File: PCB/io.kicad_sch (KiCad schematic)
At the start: 0 parts

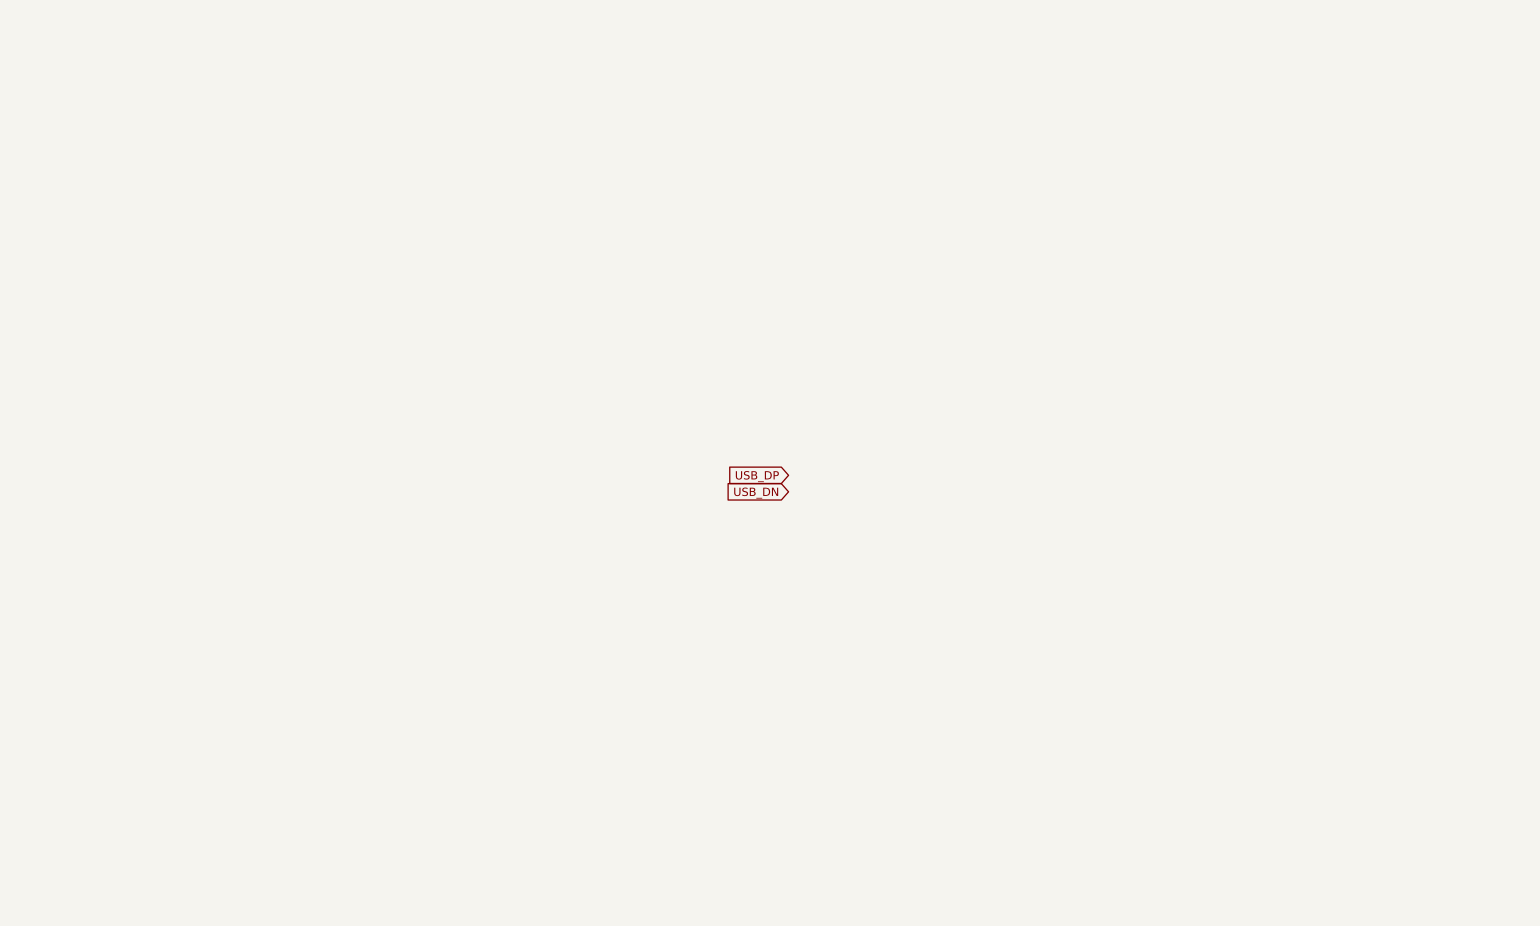
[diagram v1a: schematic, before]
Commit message: Added more components and added most needed values for the nrf example schematic
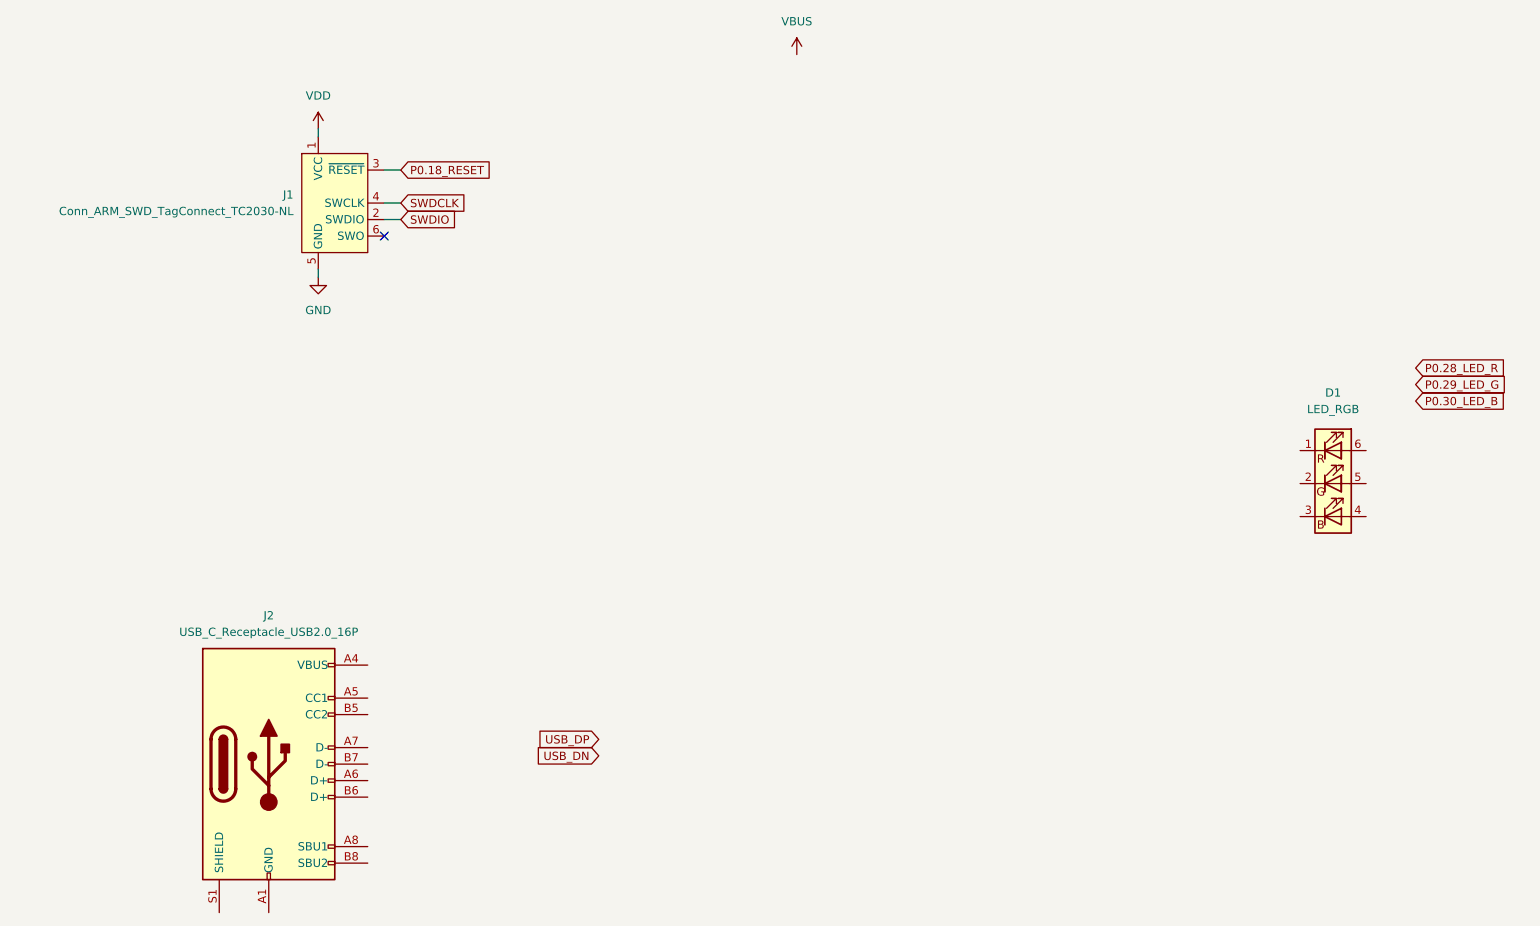
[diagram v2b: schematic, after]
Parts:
- added D1: LED_RGB, symbol Device:LED_RGB
- added J1: Conn_ARM_SWD_TagConnect_TC2030-NL, Connector:Tag-Connect_TC2030-IDC-NL_2x03_P1.27mm_Vertical, symbol Connector:Conn_ARM_SWD_TagConnect_TC2030-NL
- added J2: USB_C_Receptacle_USB2.0_16P, symbol Connector:USB_C_Receptacle_USB2.0_16P
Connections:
- new net: J2.A1 (GND), J2.A12 (GND), J2.B1 (GND), J2.B12 (GND)
- new net: J2.A4 (VBUS), J2.A9 (VBUS), J2.B4 (VBUS), J2.B9 (VBUS)
- new net GND: J1.5 (GND)
- new net P0.18_RESET: J1.3 (~{RESET})
- new net SWDCLK: J1.4 (SWCLK)
- new net SWDIO: J1.2 (SWDIO)
- new net VDD: J1.1 (VCC)
- no-connect marks 0 -> 1

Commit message: Added the Calathea Leaf as the outline and artwork for the project
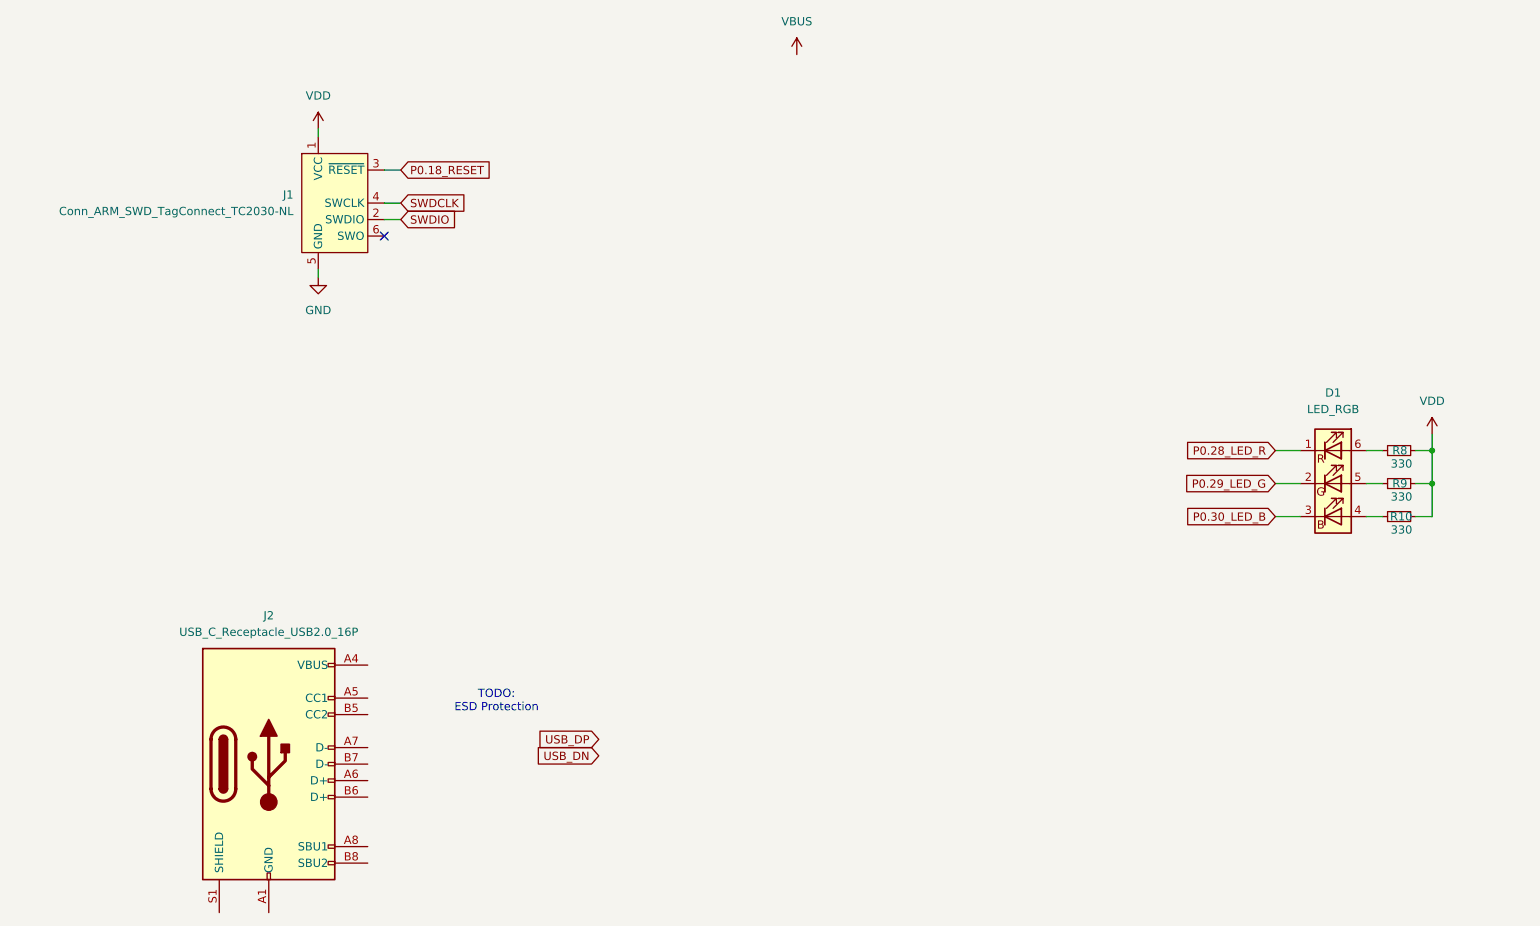
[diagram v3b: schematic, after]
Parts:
- added R10, R8, R9: 330, Resistor_SMD:R_0402_1005Metric, symbol Device:R_Small
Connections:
- net P0.28_LED_R: now also D1.1 (RK)
- net P0.29_LED_G: now also D1.2 (GK)
- net P0.30_LED_B: now also D1.3 (BK)
- net VDD: now also R10.2, R8.2, R9.2
- net at D1.4 (BA): now also R10.1
- net at D1.5 (GA): now also R9.1
- net at D1.6 (RA): now also R8.1
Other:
- note added: "TODO: ESD Protection"

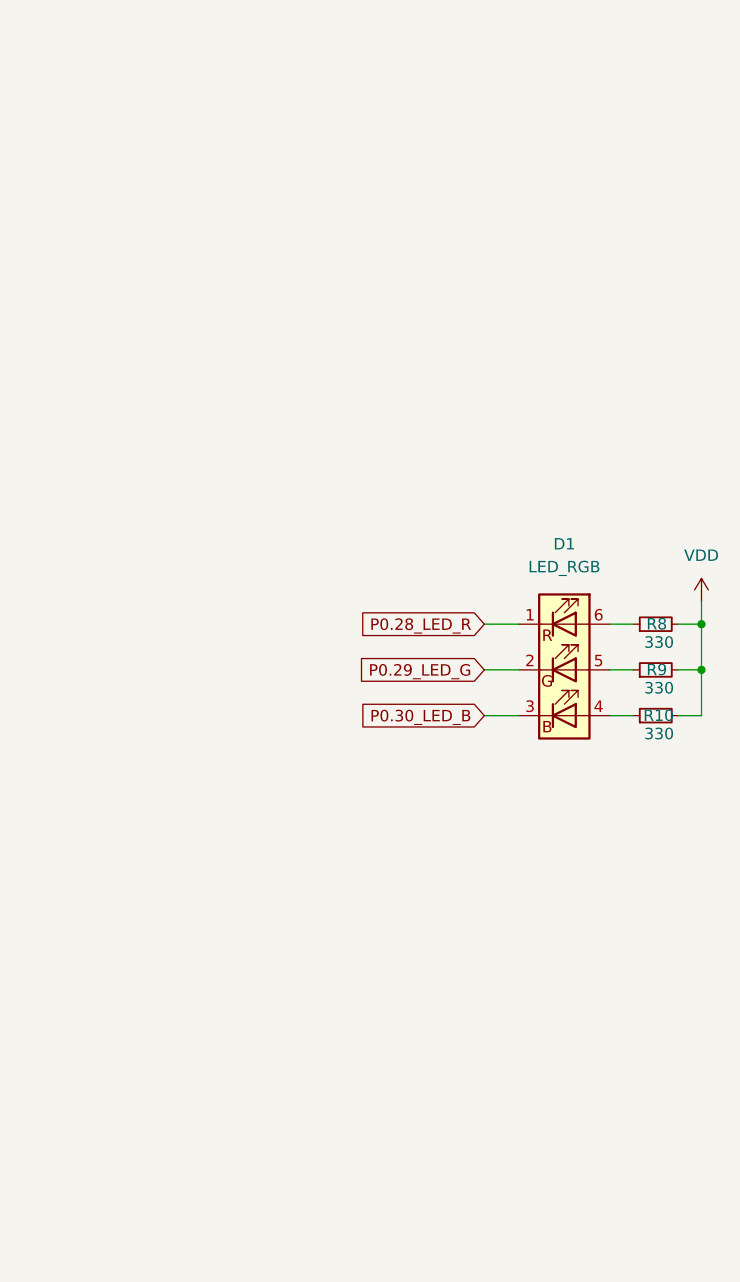
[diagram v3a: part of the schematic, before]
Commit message: Added LED Driver IC for the led bar inside the calathea leaf
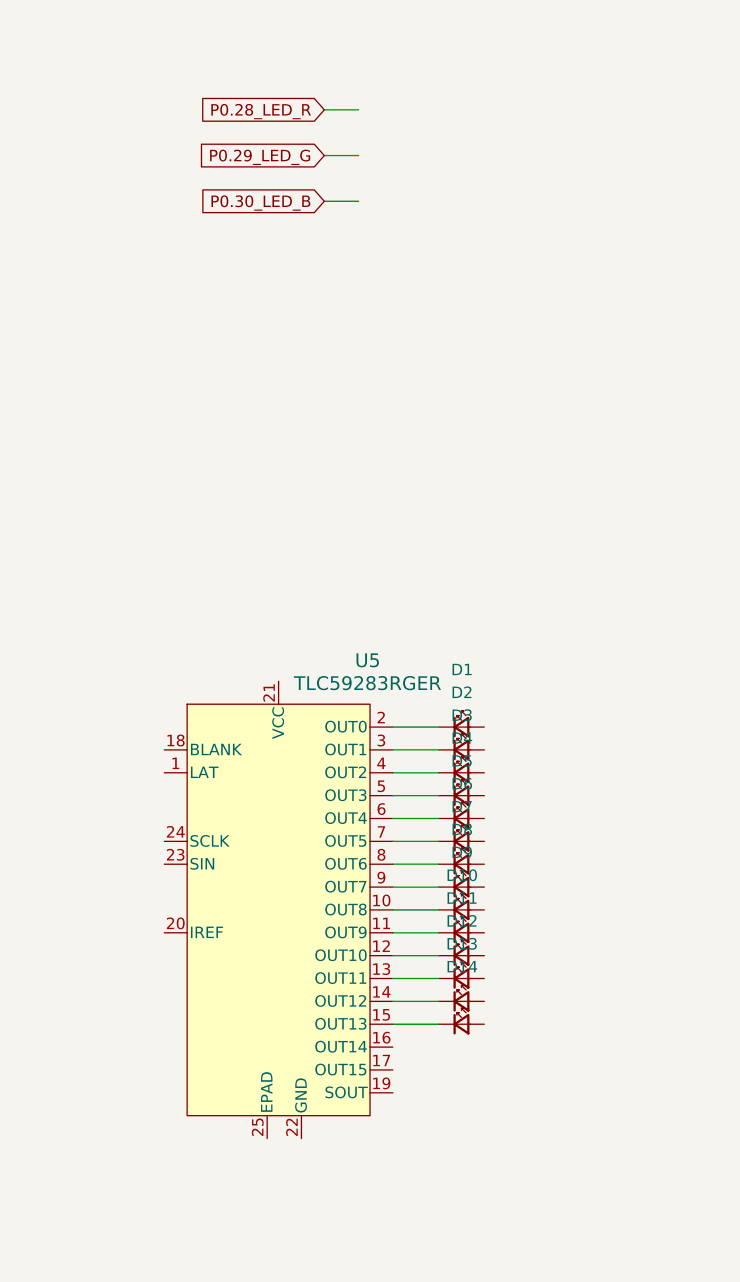
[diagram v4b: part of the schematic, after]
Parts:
- removed D1: LED_RGB, symbol Device:LED_RGB
- removed R10, R8, R9: 330, Resistor_SMD:R_0402_1005Metric, symbol Device:R_Small
- added D1, D10, D11, D12, D13, D14, D2, D3, D4, D5, D6, D7, D8, D9: LED_Small, LED_SMD:LED_0805_2012Metric, symbol Device:LED_Small
- added U5: TLC59283RGER, RGE24_2P1X2P1_TEX, symbol TLC59283:TLC59283RGER
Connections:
- new net: D7.1 (K), U5.8 (OUT6)
- new net: D8.1 (K), U5.9 (OUT7)
- new net: D6.1 (K), U5.7 (OUT5)
- new net: D3.1 (K), U5.4 (OUT2)
- new net: D5.1 (K), U5.6 (OUT4)
- new net: D1.1 (K), U5.2 (OUT0)
- new net: D2.1 (K), U5.3 (OUT1)
- new net: D9.1 (K), U5.10 (OUT8)
- new net: D10.1 (K), U5.11 (OUT9)
- new net: D11.1 (K), U5.12 (OUT10)
- new net: D12.1 (K), U5.13 (OUT11)
- new net: D13.1 (K), U5.14 (OUT12)
- new net: D14.1 (K), U5.15 (OUT13)
- new net: D4.1 (K), U5.5 (OUT3)

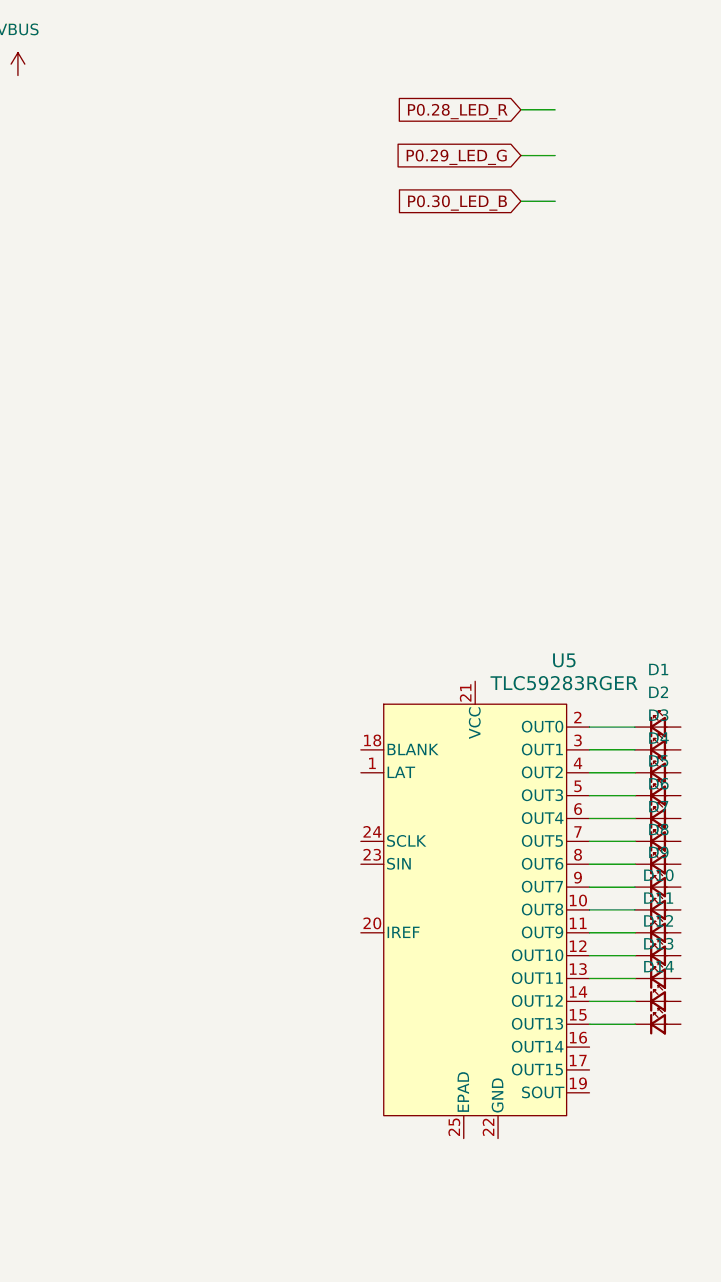
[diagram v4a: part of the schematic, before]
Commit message: added dcdc for external components. Changed board edge to a rect for easier dev board routuing.
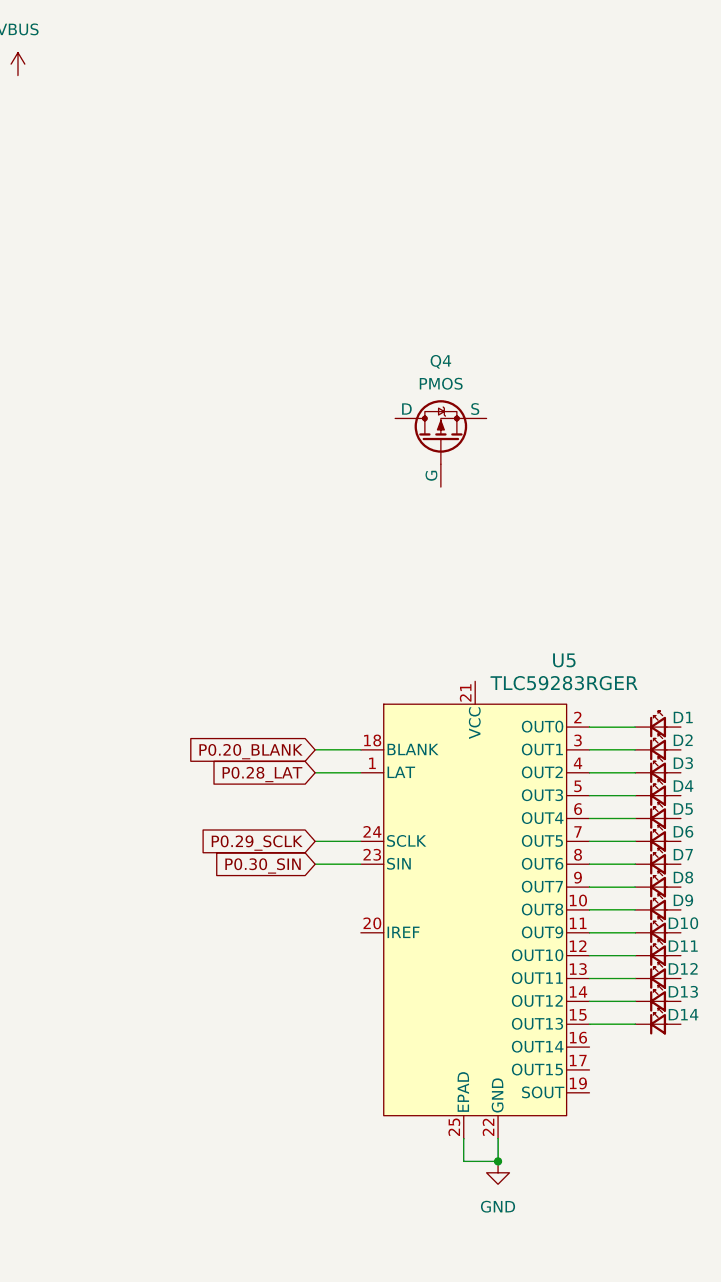
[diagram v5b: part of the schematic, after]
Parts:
- added Q4: PMOS, symbol Simulation_SPICE:PMOS
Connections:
- net GND: now also U5.22 (GND), U5.25 (EPAD)
- net P0.28_LAT: now reaches U5.1 (LAT)
- net P0.20_BLANK: now reaches U5.18 (BLANK)
- net P0.30_SIN: now reaches U5.23 (SIN)
- net P0.29_SCLK: now reaches U5.24 (SCLK)
